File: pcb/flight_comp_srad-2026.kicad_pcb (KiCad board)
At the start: 2 copper layers, 70 x 40 mm, 13 parts, among them J1 503398-1892, J2 Conn_01x04_Pin, J3 Conn_01x16_Pin, J4 Conn_01x08_Pin, J5 Conn_01x13_Pin, U1 ADXL375BCCZ-RL7, U2 MS5607-02BA, U3 RP2040, U5 MAX-M10M-00B

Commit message: added xtal
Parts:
- added Y1: Crystal, Crystal:Crystal_HC49-4H_Vertical, F.Cu at (200.6, 65.2)
- moved U1 9.41 mm to (209.7, 75.5)
- moved U2 9.35 mm to (195.9, 75.6)
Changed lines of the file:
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@@
 	(net 140 "unconnected-(U1-*CS-Pad7)")
 	(net 141 "unconnected-(U1-INT2-Pad9)")
+	(net 142 "unconnected-(Y1-Pad1)")
+	(net 143 "unconnected-(Y1-Pad2)")
 	(footprint "MountingHole:MountingHole_2.5mm"
 		(layer "F.Cu")
@@
 	(footprint "Package_LGA:LGA-8_3x5mm_P1.25mm"
 		(layer "F.Cu")
-		(at 197.575 66.425001)
+		(at 195.925 75.625)
 		(descr "LGA-8")
 		(tags "lga land grid array")
@@
 		(embedded_fonts no)
 	)
+	(footprint "Crystal:Crystal_HC49-4H_Vertical"
+		(layer "F.Cu")
+		(at 200.62 65.25)
+		(descr "HC-49-4H, Crystal, http://5hertz.com/pdfs/04404_D.pdf")
+		(property "Reference" "Y1"
+			(at 2.44 -3.52 0)
+			(layer "F.SilkS")
+			(effects
+				(font
+					(size 1 1)
+					(thickness 0.15)
+				)
+			)
+		)
+		(property "Value" "Crystal"
+			(at 2.44 3.52 0)
+			(layer "F.Fab")
+			(effects
+				(font
+					(size 1 1)
+					(thickness 0.15)
+				)
+			)
+		)
+		(property "Datasheet" "~"
+			(at 0 0 0)
+			(layer "F.Fab")
+			(hide yes)
+			(effects
+				(font
+					(size 1.27 1.27)
+					(thickness 0.15)
+				)
+			)
+		)
+		(property "Description" "Two pin crystal"
+			(at 0 0 0)
+			(layer "F.Fab")
+			(hide yes)
+			(effects
+				(font
+					(size 1.27 1.27)
+					(thickness 0.15)
+				)
+			)
+		)
+		(property ki_fp_filters "Crystal*")
+		(sheetname "/")
+		(sheetfile "flight_comp_srad-2026.kicad_sch")
+		(attr through_hole)
+		(fp_line
+			(start -0.76 -2.435)
+			(end 5.64 -2.435)
+			(stroke
+				(width 0.12)
+				(type solid)
+			)
+			(layer "F.SilkS")
+		)
+		(fp_line
+			(start 5.64 2.435)
+			(end -0.76 2.435)
+			(stroke
+				(width 0.12)
+				(type solid)
+			)
+			(layer "F.SilkS")
+		)
+		(fp_arc
+			(start -0.76 2.435)
+			(mid -3.195 0)
+			(end -0.76 -2.435)
+			(stroke
+				(width 0.12)
+				(type solid)
+			)
+			(layer "F.SilkS")
+		)
+		(fp_arc
+			(start 5.64 -2.435)
+			(mid 8.075 0)
+			(end 5.64 2.435)
+			(stroke
+				(width 0.12)
+				(type solid)
+			)
+			(layer "F.SilkS")
+		)
+		(fp_line
+			(start -0.76 -2.83)
+			(end 5.64 -2.83)
+			(stroke
+				(width 0.05)
+				(type solid)
+			)
+			(layer "F.CrtYd")
+		)
+		(fp_line
+			(start 5.64 2.83)
+			(end -0.76 2.83)
+			(stroke
+				(width 0.05)
+				(type solid)
+			)
+			(layer "F.CrtYd")
+		)
+		(fp_arc
+			(start -0.76 2.83)
+			(mid -3.59 0)
+			(end -0.76 -2.83)
+			(stroke
+				(width 0.05)
+				(type solid)
+			)
+			(layer "F.CrtYd")
+		)
+		(fp_arc
+			(start 5.64 -2.83)
+			(mid 8.47 0)
+			(end 5.64 2.83)
+			(stroke
+				(width 0.05)
+				(type solid)
+			)
+			(layer "F.CrtYd")
+		)
+		(fp_line
+			(start -0.76 -2.325)
+			(end 5.64 -2.325)
+			(stroke
+				(width 0.1)
+				(type solid)
+			)
+			(layer "F.Fab")
+		)
+		(fp_line
+			(start 5.64 2.325)
+			(end -0.76 2.325)
+			(stroke
+				(width 0.1)
+				(type solid)
+			)
+			(layer "F.Fab")
+		)
+		(fp_arc
+			(start -0.76 2.325)
+			(mid -3.085 0)
+			(end -0.76 -2.325)
+			(stroke
+				(width 0.1)
+				(type solid)
+			)
+			(layer "F.Fab")
+		)
+		(fp_arc
+			(start 5.64 -2.325)
+			(mid 7.965 0)
+			(end 5.64 2.325)
+			(stroke
+				(width 0.1)
+				(type solid)
+			)
+			(layer "F.Fab")
+		)
+		(fp_text user "${REFERENCE}"
+			(at 2.44 0 0)
+			(layer "F.Fab")
+			(effects
+				(font
+					(size 1 1)
+					(thickness 0.15)
+				)
+			)
+		)
+		(pad "1" thru_hole circle
+			(at 0 0)
+			(size 1.5 1.5)
+			(drill 0.8)
+			(layers "*.Cu" "*.Mask")
+			(remove_unused_layers no)
+			(net 142 "unconnected-(Y1-Pad1)")
+			(pinfunction "1")
+			(pintype "passive")
+		)
+		(pad "2" thru_hole circle
+			(at 4.88 0)
+			(size 1.5 1.5)
+			(drill 0.8)
+			(layers "*.Cu" "*.Mask")
+			(remove_unused_layers no)
+			(net 143 "unconnected-(Y1-Pad2)")
+			(pinfunction "2")
+			(pintype "passive")
+		)
+		(embedded_fonts no)
+		(model "${KICAD9_3DMODEL_DIR}/Crystal.3dshapes/Crystal_HC49-4H_Vertical.step"
+			(offset
+				(xyz 0 0 0)
+			)
+			(scale
+				(xyz 1 1 1)
+			)
+			(rotate
+				(xyz 0 0 0)
+			)
+		)
+	)
 	(footprint "Connector_PinHeader_2.00mm:PinHeader_1x08_P2.00mm_Vertical"
 		(layer "F.Cu")
@@
 		(tags "QFN NoLead")
 		(property "Reference" "U3"
-			(at -0.641804 -4.83 -0)
+			(at -0.641804 -4.83 0)
 			(layer "B.SilkS")
 			(effects
@@
 	(footprint "SRAD_fligh_comp2026:ADXL375BCCZ-RL7-L"
 		(layer "F.Cu")
-		(at 207.679899 66.3)
+		(at 209.679899 75.499999)
 		(tags "ADXL375BCCZ-RL7 ")
 		(property "Reference" "U1"

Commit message: mas cosas al schem
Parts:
- added C1: 15p, TCLib:C_0805, F.Cu at (201.2, 108.8)
- added C10: 1u, Capacitor_SMD:C_0805_2012Metric, F.Cu at (187.8, 111.8)
- added C11: 100n, Capacitor_SMD:C_0805_2012Metric, F.Cu at (187.8, 114.8)
- added C12: 100n, Capacitor_SMD:C_0805_2012Metric, F.Cu at (187.8, 117.8)
- added C13: 100n, Capacitor_SMD:C_0805_2012Metric, F.Cu at (187.8, 120.8)
- added C14: 100n, Capacitor_SMD:C_0805_2012Metric, F.Cu at (187.8, 123.8)
- added C15: 100n, Capacitor_SMD:C_0805_2012Metric, F.Cu at (192.2, 108.8)
- added C16: 100n, Capacitor_SMD:C_0805_2012Metric, F.Cu at (192.2, 111.8)
- added C17: 10u, Capacitor_SMD:C_0805_2012Metric, F.Cu at (192.2, 114.8)
- added C2: 15p, TCLib:C_0805, F.Cu at (201.2, 111.8)
- added C3: 10u, Capacitor_SMD:C_0805_2012Metric, F.Cu at (183.3, 108.8)
- added C4: 10u, Capacitor_SMD:C_0805_2012Metric, F.Cu at (183.3, 111.8)
- added C5: 100n, Capacitor_SMD:C_0805_2012Metric, F.Cu at (183.3, 114.8)
- added C6: 100n, Capacitor_SMD:C_0805_2012Metric, F.Cu at (183.3, 117.8)
- added C7: 100n, Capacitor_SMD:C_0805_2012Metric, F.Cu at (183.3, 120.8)
- added C8: 1u, Capacitor_SMD:C_0805_2012Metric, F.Cu at (183.3, 123.8)
- added C9: 100n, Capacitor_SMD:C_0805_2012Metric, F.Cu at (187.8, 108.8)
- added R0: DNF, Resistor_SMD:R_0805_2012Metric, F.Cu at (196.6, 108.7)
- added R1: 1k, TCLib:R_0805, F.Cu at (201.2, 114.7)
- added R2: 1k, Resistor_SMD:R_0805_2012Metric, F.Cu at (196.6, 111.7)
- added R3: 27, Resistor_SMD:R_0805_2012Metric, F.Cu at (196.6, 114.6)
- added R4: 27, Resistor_SMD:R_0805_2012Metric, F.Cu at (196.6, 117.6)
- added U4: NCP1117-3.3_SOT223, Package_TO_SOT_SMD:SOT-223-3_TabPin2, F.Cu at (199.3, 123.2)
- added U6: W25Q128JVS, Package_SO:SOIC-8_5.3x5.3mm_P1.27mm, F.Cu at (186.2, 128.8)
- J1: footprint flight_computer:503398-1892-1 -> SRAD_fligh_comp2026:503398-1892-1
- U3: footprint Package_DFN_QFN:QFN-56-1EP_7x7mm_P0.4mm_EP3.2x3.2mm -> SRAD_fligh_comp2026:RP2040-QFN-56
- moved U3 0.79 mm to (203.1, 76.4)
- moved J1 0.17 mm to (196.5, 81.6)
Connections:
- J2 pad 1: unconnected-(J2-Pin_1-Pad1) -> 5V
- J2 pad 2: unconnected-(J2-Pin_2-Pad2) -> /TX
- J2 pad 3: unconnected-(J2-Pin_3-Pad3) -> /RX
- J2 pad 4: unconnected-(J2-Pin_4-Pad4) -> GND
- U3 pad 1: Net-(U3-IOVDD-Pad1) -> +3V3
- U3 pad 10: Net-(U3-IOVDD-Pad1) -> +3V3
- U3 pad 19: unconnected-(U3-TESTEN-Pad19) -> GND
- U3 pad 20: unconnected-(U3-XIN-Pad20) -> /XIN
- U3 pad 21: unconnected-(U3-XOUT-Pad21) -> /XOUT
- U3 pad 22: Net-(U3-IOVDD-Pad1) -> +3V3
- U3 pad 23: Net-(U3-DVDD-Pad23) -> +1V1
- U3 pad 33: Net-(U3-IOVDD-Pad1) -> +3V3
- U3 pad 42: Net-(U3-IOVDD-Pad1) -> +3V3
- U3 pad 43: unconnected-(U3-ADC_AVDD-Pad43) -> +3V3
- U3 pad 44: unconnected-(U3-VREG_IN-Pad44) -> +3V3
- U3 pad 45: unconnected-(U3-VREG_VOUT-Pad45) -> +1V1
- U3 pad 48: unconnected-(U3-USB_VDD-Pad48) -> +3V3
- U3 pad 49: Net-(U3-IOVDD-Pad1) -> +3V3
- U3 pad 50: Net-(U3-DVDD-Pad23) -> +1V1
- U3 pad 51: unconnected-(U3-QSPI_SD3-Pad51) -> /QSPI_SD3
- U3 pad 52: unconnected-(U3-QSPI_SCLK-Pad52) -> /QSPI_SCLK
- U3 pad 53: unconnected-(U3-QSPI_SD0-Pad53) -> /QSPI_SD0
- U3 pad 54: unconnected-(U3-QSPI_SD2-Pad54) -> /QSPI_SD2
- U3 pad 55: unconnected-(U3-QSPI_SD1-Pad55) -> /QSPI_SD1
- U3 pad 56: unconnected-(U3-QSPI_SS-Pad56) -> /QSPI_SS
- U3 pad 57: unconnected-(U3-GND-Pad57) -> GND
- Y1 pad 1: unconnected-(Y1-Pad1) -> Net-(C2-Pad2)
- Y1 pad 2: unconnected-(Y1-Pad2) -> /XIN

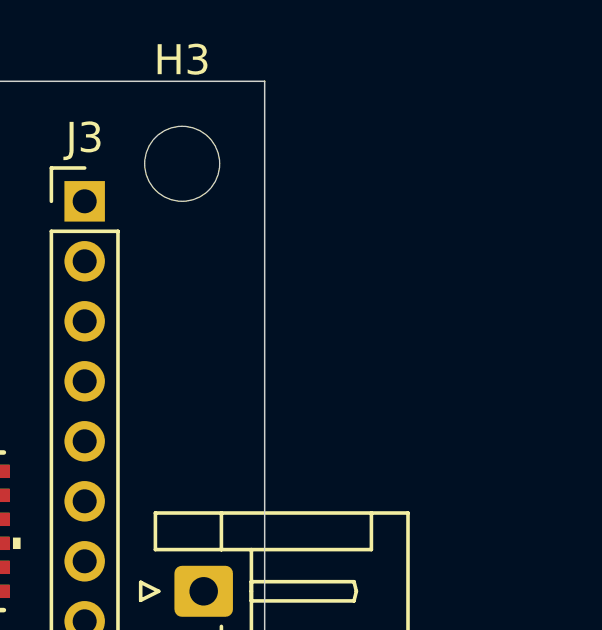
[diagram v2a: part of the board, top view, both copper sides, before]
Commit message: nuevos componentes menos xtal
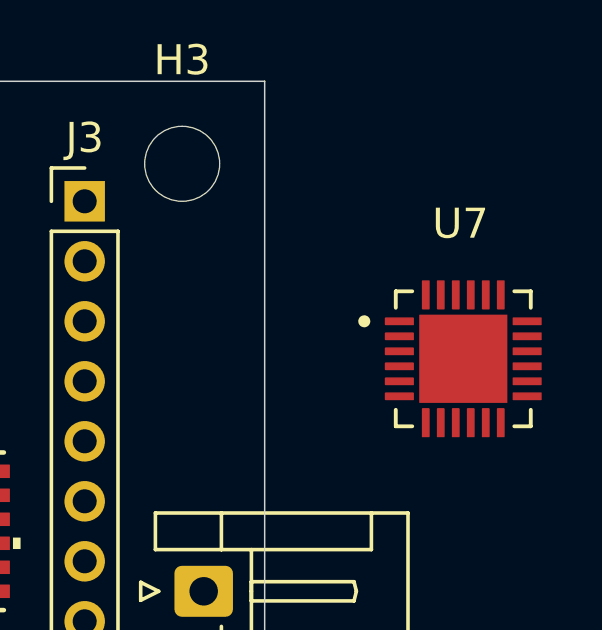
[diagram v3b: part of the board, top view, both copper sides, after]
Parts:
- added U7: IIM-20670, IIM-20670:QFN50P450X450X115-25N, F.Cu at (226.6, 69.8)

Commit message: xtal smd
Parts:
- Y1: value Crystal -> ABM8-272-T3; footprint Crystal:Crystal_HC49-4H_Vertical -> ABM8_272_T3:XTAL_ABM8-272-T3
- moved U7 19.6 mm to (207.5, 65.6)
- moved Y1 2.03 mm to (200.2, 67.2)
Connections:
- Y1 pad 1: Net-(C2-Pad2) -> /XIN
- Y1 pad 2: /XIN -> GND

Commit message: agregue xbee footprint, symb y .step
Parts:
- removed J3: Conn_01x16_Pin, Connector_PinHeader_2.00mm:PinHeader_1x16_P2.00mm_Vertical
- removed J4: Conn_01x08_Pin, Connector_PinHeader_2.00mm:PinHeader_1x08_P2.00mm_Vertical
- removed J5: Conn_01x13_Pin, Connector_PinHeader_2.00mm:PinHeader_1x13_P2.00mm_Vertical
- added U9: XBP9B-DMSTB002, SRAD_fligh_comp2026:XBEEPRO, F.Cu at (203.0, 83.5)

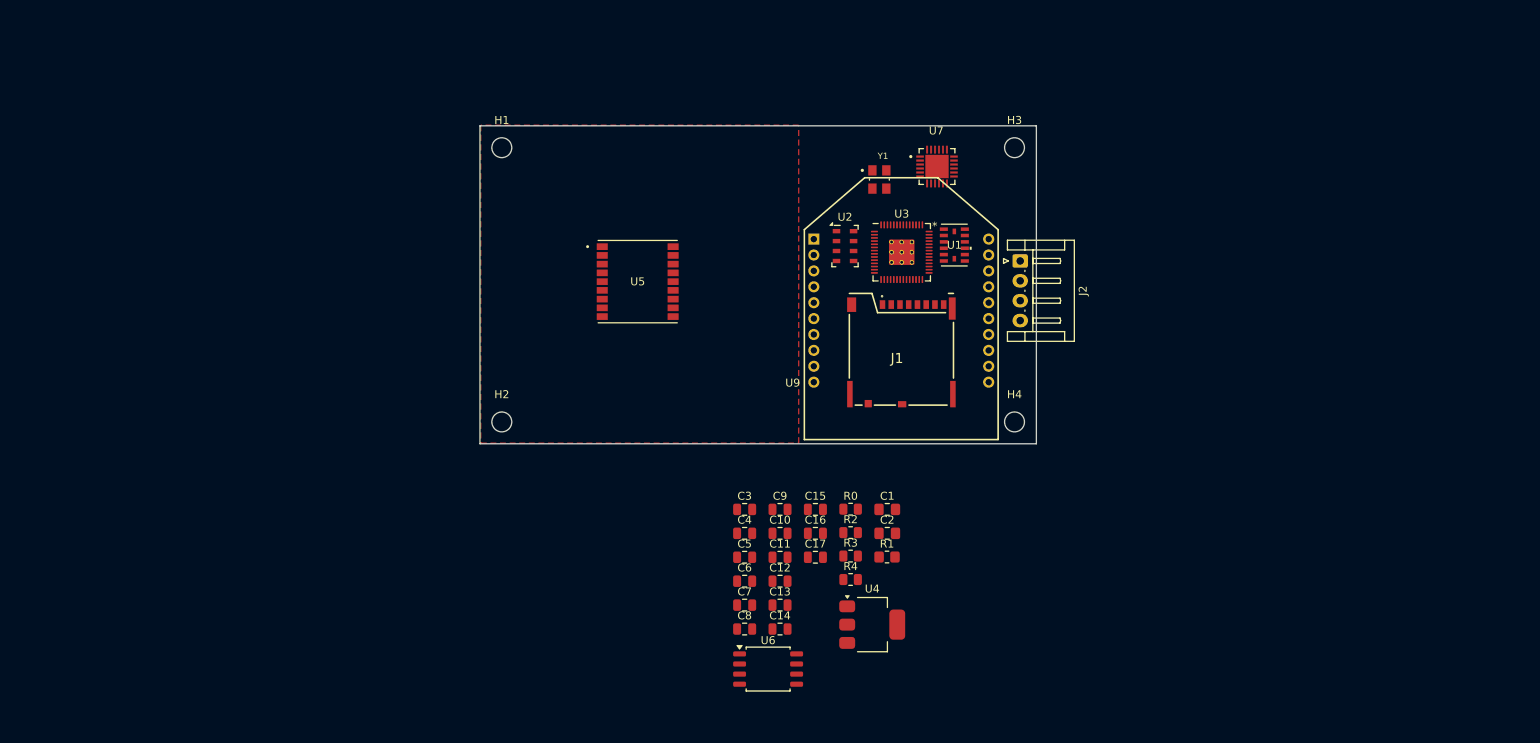
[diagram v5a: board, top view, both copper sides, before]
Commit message: schematic del rp2040 hecho
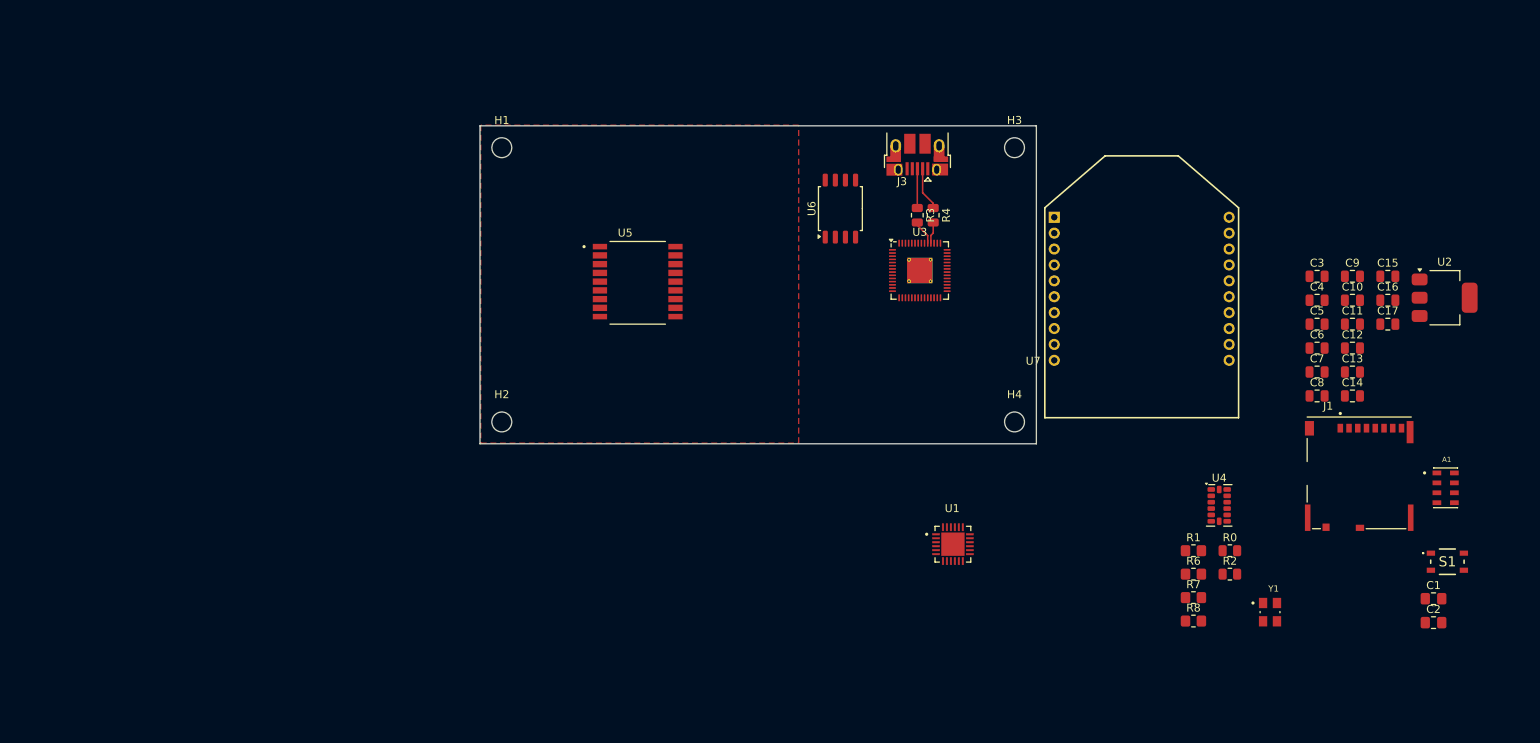
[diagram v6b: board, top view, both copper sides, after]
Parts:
- removed J2: Conn_01x04_Pin, Connector_JST:JST_EH_S4B-EH_1x04_P2.50mm_Horizontal
- removed U9: XBP9B-DMSTB002, SRAD_fligh_comp2026:XBEEPRO
- added A1: MS561101BA03-50, MS561101BA03_50:XDCR_MS561101BA03-50, F.Cu at (271.5, 106.0)
- added J3: USB_B_Micro, Connector_USB:USB_Micro-B_Amphenol_10103594-0001LF_Horizontal, F.Cu at (205.0, 64.1)
- added R6: 10k, Resistor_SMD:R_0805_2012Metric_Pad1.20x1.40mm_HandSolder, F.Cu at (239.8, 116.9)
- added R7: 10k, Resistor_SMD:R_0805_2012Metric_Pad1.20x1.40mm_HandSolder, F.Cu at (239.8, 119.8)
- added R8: DNF, Resistor_SMD:R_0805_2012Metric_Pad1.20x1.40mm_HandSolder, F.Cu at (239.8, 122.8)
- added S1: PTS810SJK250SMTR_LFS, PTS810SJK250SMTRLFS:PTS810SJK250SMTRLFS, F.Cu at (271.7, 115.3)
- J1: footprint SRAD_fligh_comp2026:503398-1892-1 -> 5033981892:MOLEX_503398-1892
- R1: footprint TCLib:R_0805 -> Resistor_SMD:R_0805_2012Metric_Pad1.20x1.40mm_HandSolder
- U1: value ADXL375BCCZ-RL7 -> IIM-20670; footprint SRAD_fligh_comp2026:ADXL375BCCZ-RL7-L -> IIM_20670:QFN50P450X450X115-25N
- U2: value MS5607-02BA -> NCP1117-3.3_SOT223; footprint Package_LGA:LGA-8_3x5mm_P1.25mm -> Package_TO_SOT_SMD:SOT-223-3_TabPin2
- U3: footprint SRAD_fligh_comp2026:RP2040-QFN-56 -> Package_DFN_QFN:QFN-56-1EP_7x7mm_P0.4mm_EP3.2x3.2mm_ThermalVias
- U4: value NCP1117-3.3_SOT223 -> ADXL375BCCZ-RL7; footprint Package_TO_SOT_SMD:SOT-223-3_TabPin2 -> Package_LGA:LGA-14_3x5mm_P0.8mm_LayoutBorder1x6y
- U5: footprint SRAD_fligh_comp2026:MOD18_MAX-M10M_UBL -> MAX_M10M_00B:XCVR_MAX-M10M-00B
- U7: value IIM-20670 -> XBP9B-DMSTB002; footprint IIM-20670:QFN50P450X450X115-25N -> XBEEPRO:XBEEPRO
- moved C10 77.8 mm to (259.8, 82.4)
- moved C11 77.8 mm to (259.8, 85.5)
- moved C12 77.8 mm to (259.8, 88.5)
- moved C13 77.8 mm to (259.8, 91.5)
- moved C14 77.8 mm to (259.8, 94.5)
- moved C15 77.8 mm to (264.2, 79.4)
- moved C16 77.8 mm to (264.2, 82.4)
- moved C17 77.8 mm to (264.2, 85.5)
- moved C3 77.8 mm to (255.3, 79.4)
- moved C4 77.8 mm to (255.3, 82.4)
- moved C5 77.8 mm to (255.3, 85.5)
- moved C6 77.8 mm to (255.3, 88.5)
- moved C7 77.8 mm to (255.3, 91.5)
- moved C8 77.8 mm to (255.3, 94.5)
- moved C9 77.8 mm to (259.8, 79.4)
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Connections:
- C3 pad 1: 5V -> VBUS
- C4 pad 1: 3V3 -> +3V3
- J1 pad 1: unconnected-(J1-DAT2-Pad1) -> /SD_DAT2
- J1 pad 10: unconnected-(J1-DETECT_SWITCH-Pad10) -> /SD_DS
- J1 pad 2: unconnected-(J1-CD/DAT3-Pad2) -> /SD_DAT3
- J1 pad 3: unconnected-(J1-CMD-Pad3) -> /SD_CMD
- J1 pad 4: unconnected-(J1-VDD-Pad4) -> +3V3
- J1 pad 5: unconnected-(J1-CLK-Pad5) -> /SD_CLK
- J1 pad 6: unconnected-(J1-VSS-Pad6) -> GND
- J1 pad 7: unconnected-(J1-DAT0-Pad7) -> /SD_DAT0
- J1 pad 8: unconnected-(J1-DAT1-Pad8) -> /SD_DAT1
- J1 pad 9: unconnected-(J1-DETECT_LEVER-Pad9) -> GND
- R3 pad 2: unconnected-(R3-Pad2) -> Net-(U3-USB_DP)
- R4 pad 2: unconnected-(R4-Pad2) -> Net-(U3-USB_DM)
- U2 pad 1: unconnected-(U2-VDD-Pad1) -> GND
- U2 pad 2: unconnected-(U2-PS-Pad2) -> +3V3
- U2 pad 3: unconnected-(U2-GND-Pad3) -> VBUS
- U3 pad 29: unconnected-(U3-GPIO18-Pad29) -> /SD_CMD
- U3 pad 30: unconnected-(U3-GPIO19-Pad30) -> /SD_DAT0
- U3 pad 31: unconnected-(U3-GPIO20-Pad31) -> /SD_DAT1
- U3 pad 32: unconnected-(U3-GPIO21-Pad32) -> /SD_DAT2
- U3 pad 34: unconnected-(U3-GPIO22-Pad34) -> /SD_DAT3
- U3 pad 46: unconnected-(U3-USB_DM-Pad46) -> Net-(U3-USB_DM)
- U3 pad 47: unconnected-(U3-USB_DP-Pad47) -> Net-(U3-USB_DP)
- U4 pad 1: GND -> unconnected-(U4-VDDI/O-Pad1)
- U4 pad 2: 3V3 -> unconnected-(U4-GND-Pad2)
- U4 pad 3: 5V -> unconnected-(U4-RESERVED-Pad3)
- U7 pad 14: GND -> unconnected-(U7-VREF-Pad14)
- U7 pad 15: GND -> unconnected-(U7-ASSOCIATE/DIO5-Pad15)
- U7 pad 16: GND -> unconnected-(U7-NRTS/DIO6-Pad16)
- U7 pad 17: GND -> unconnected-(U7-AD3/DIO3/SPI_NSSEL-Pad17)
- U7 pad 2: GND -> unconnected-(U7-DOUT/DIO13-Pad2)
- U7 pad 3: GND -> unconnected-(U7-DIN/NCONFIG/DIO14-Pad3)
- U7 pad 4: GND -> unconnected-(U7-DIO12/SPI_MISO-Pad4)
- U7 pad 5: GND -> unconnected-(U7-~{RESET}-Pad5)
- U7 pad 7: GND -> unconnected-(U7-DIO11/PWM1-Pad7)
- U7 pad 8: unconnected-(U7-VDDIO-Pad8) -> (no net)
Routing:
- net /USB_D-: track 0.00 -> 5.49 mm
- net /USB_D+: track 0.00 -> 4.95 mm
- net Net-(U3-USB_DP): track 0.00 -> 3.14 mm
- net Net-(U3-USB_DM): track 0.00 -> 2.72 mm
- added copper zone on F.Cu, net GND
- removed copper zone on F.Cu, net (none)
